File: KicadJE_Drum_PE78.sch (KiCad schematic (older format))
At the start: 112 parts, among them J101 Snare, J102 LCymbals, J103 SCymbals, J104 Maracas, J105 Bass, J106 LBongo, J107 HBongo, J108 Claves, P101 HEADER_2x8_Doepfer, Q101 2N3904, Q102 2N3904, Q103 2N3904, Q104 2N3904, U101 74HC04

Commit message: Faceplate etc
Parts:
- P101: footprint HEADER_2x8 -> Connector_IDC:IDC-Header_2x08_P2.54mm_Vertical
- U101: footprint AJ:AJ_SO-14_5.3x6.2mm_P1.27mm -> Package_SO:SO-14_5.3x10.2mm_P1.27mm
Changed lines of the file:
@@
 F 0 "U101" H 3875 1042 50  0000 C CNN
 F 1 "74HC04" H 3875 951 50  0000 C CNN
-F 2 "AJ:AJ_SO-14_5.3x6.2mm_P1.27mm" H 3875 725 50  0001 C CNN
+F 2 "Package_SO:SO-14_5.3x10.2mm_P1.27mm" H 3875 725 50  0001 C CNN
 F 3 "https://assets.nexperia.com/documents/data-sheet/74HC_HCT04.pdf" H 3875 725 50  0001 C CNN
 	1    3875 725
@@
 F 0 "U101" H 8500 1042 50  0000 C CNN
 F 1 "74HC04" H 8500 951 50  0000 C CNN
-F 2 "AJ:AJ_SO-14_5.3x6.2mm_P1.27mm" H 8500 725 50  0001 C CNN
+F 2 "Package_SO:SO-14_5.3x10.2mm_P1.27mm" H 8500 725 50  0001 C CNN
 F 3 "https://assets.nexperia.com/documents/data-sheet/74HC_HCT04.pdf" H 8500 725 50  0001 C CNN
 	2    8500 725
@@
 F 0 "U101" H 3875 2867 50  0000 C CNN
 F 1 "74HC04" H 3875 2776 50  0000 C CNN
-F 2 "AJ:AJ_SO-14_5.3x6.2mm_P1.27mm" H 3875 2550 50  0001 C CNN
+F 2 "Package_SO:SO-14_5.3x10.2mm_P1.27mm" H 3875 2550 50  0001 C CNN
 F 3 "https://assets.nexperia.com/documents/data-sheet/74HC_HCT04.pdf" H 3875 2550 50  0001 C CNN
 	3    3875 2550
@@
 F 0 "U101" H 8450 2842 50  0000 C CNN
 F 1 "74HC04" H 8450 2751 50  0000 C CNN
-F 2 "AJ:AJ_SO-14_5.3x6.2mm_P1.27mm" H 8450 2525 50  0001 C CNN
+F 2 "Package_SO:SO-14_5.3x10.2mm_P1.27mm" H 8450 2525 50  0001 C CNN
 F 3 "https://assets.nexperia.com/documents/data-sheet/74HC_HCT04.pdf" H 8450 2525 50  0001 C CNN
 	4    8450 2525
@@
 F 0 "U101" H 10905 5621 50  0000 L CNN
 F 1 "74HC04" H 10905 5530 50  0000 L CNN
-F 2 "AJ:AJ_SO-14_5.3x6.2mm_P1.27mm" H 10675 5575 50  0001 C CNN
+F 2 "Package_SO:SO-14_5.3x10.2mm_P1.27mm" H 10675 5575 50  0001 C CNN
 F 3 "https://assets.nexperia.com/documents/data-sheet/74HC_HCT04.pdf" H 10675 5575 50  0001 C CNN
 	7    10675 5575
@@
 F 0 "P101" H 8025 4977 40  0000 C CNN
 F 1 "HEADER_2x8_Doepfer" H 8025 5053 40  0000 C CNN
-F 2 "HEADER_2x8" H 8025 5144 60  0000 C CNN
+F 2 "Connector_IDC:IDC-Header_2x08_P2.54mm_Vertical" H 8025 5144 60  0000 C CNN
 F 3 "" H 8025 5675 60  0000 C CNN
 	1    8025 5675

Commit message: Powerfootprintupdated
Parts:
- C101, C102, C103, C104, C105, C106, C107, C108, C109, C110, C111, C112, C113, C114, C115, C116, C117, C118, C119, C120, C121, C122, C123, C124, C125, C126, C127, C128, C129, C130: footprint Capacitor_SMD:C_1206_3216Metric_Pad1.42x1.75mm_HandSolder -> AJ:C_0805_AJ
- RV102: value R_POT -> 220k
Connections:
- net -12: now reaches D109.1 (K), P101.1 (-12), P101.2 (-12), R145.2
- net +12: now reaches P101.10 (+12), P101.9 (+12), R151.2
- net +5: now reaches P101.11 (+5), P101.12 (+5), R146.2
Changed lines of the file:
@@
 F 0 "C128" H 8890 6021 50  0000 L CNN
 F 1 "1u" H 8890 5930 50  0000 L CNN
-F 2 "Capacitor_SMD:C_1206_3216Metric_Pad1.42x1.75mm_HandSolder" H 8813 5825 50  0001 C CNN
+F 2 "AJ:C_0805_AJ" H 8813 5825 50  0001 C CNN
 F 3 "~" H 8775 5975 50  0001 C CNN
 	1    8775 5975
@@
 F 0 "C127" H 8890 5621 50  0000 L CNN
 F 1 "1u" H 8890 5530 50  0000 L CNN
-F 2 "Capacitor_SMD:C_1206_3216Metric_Pad1.42x1.75mm_HandSolder" H 8813 5425 50  0001 C CNN
+F 2 "AJ:C_0805_AJ" H 8813 5425 50  0001 C CNN
 F 3 "~" H 8775 5575 50  0001 C CNN
 	1    8775 5575
@@
 F 0 "C113" H 3940 1546 50  0000 L CNN
 F 1 "150n" H 3940 1455 50  0000 L CNN
-F 2 "Capacitor_SMD:C_1206_3216Metric_Pad1.42x1.75mm_HandSolder" H 3863 1350 50  0001 C CNN
+F 2 "AJ:C_0805_AJ" H 3863 1350 50  0001 C CNN
 F 3 "~" H 3825 1500 50  0001 C CNN
 	1    3825 1500
@@
 F 0 "C109" H 3690 1871 50  0000 L CNN
 F 1 "47n" H 3690 1780 50  0000 L CNN
-F 2 "Capacitor_SMD:C_1206_3216Metric_Pad1.42x1.75mm_HandSolder" H 3613 1675 50  0001 C CNN
+F 2 "AJ:C_0805_AJ" H 3613 1675 50  0001 C CNN
 F 3 "~" H 3575 1825 50  0001 C CNN
 	1    3575 1825
@@
 F 0 "C115" H 4140 1871 50  0000 L CNN
 F 1 "47n" H 4140 1780 50  0000 L CNN
-F 2 "Capacitor_SMD:C_1206_3216Metric_Pad1.42x1.75mm_HandSolder" H 4063 1675 50  0001 C CNN
+F 2 "AJ:C_0805_AJ" H 4063 1675 50  0001 C CNN
 F 3 "~" H 4025 1825 50  0001 C CNN
 	1    4025 1825
@@
 F 0 "C123" H 8540 1546 50  0000 L CNN
 F 1 "33n" H 8540 1455 50  0000 L CNN
-F 2 "Capacitor_SMD:C_1206_3216Metric_Pad1.42x1.75mm_HandSolder" H 8463 1350 50  0001 C CNN
+F 2 "AJ:C_0805_AJ" H 8463 1350 50  0001 C CNN
 F 3 "~" H 8425 1500 50  0001 C CNN
 	1    8425 1500
@@
 F 0 "C121" H 8290 1871 50  0000 L CNN
 F 1 "10n" H 8290 1780 50  0000 L CNN
-F 2 "Capacitor_SMD:C_1206_3216Metric_Pad1.42x1.75mm_HandSolder" H 8213 1675 50  0001 C CNN
+F 2 "AJ:C_0805_AJ" H 8213 1675 50  0001 C CNN
 F 3 "~" H 8175 1825 50  0001 C CNN
 	1    8175 1825
@@
 F 0 "C125" H 8740 1871 50  0000 L CNN
 F 1 "10n" H 8740 1780 50  0000 L CNN
-F 2 "Capacitor_SMD:C_1206_3216Metric_Pad1.42x1.75mm_HandSolder" H 8663 1675 50  0001 C CNN
+F 2 "AJ:C_0805_AJ" H 8663 1675 50  0001 C CNN
 F 3 "~" H 8625 1825 50  0001 C CNN
 	1    8625 1825
@@
 F 0 "C124" H 8540 3346 50  0000 L CNN
 F 1 "4n7" H 8540 3255 50  0000 L CNN
-F 2 "Capacitor_SMD:C_1206_3216Metric_Pad1.42x1.75mm_HandSolder" H 8463 3150 50  0001 C CNN
+F 2 "AJ:C_0805_AJ" H 8463 3150 50  0001 C CNN
 F 3 "~" H 8425 3300 50  0001 C CNN
 	1    8425 3300
@@
 F 0 "C122" H 8290 3671 50  0000 L CNN
 F 1 "1n5" H 8290 3580 50  0000 L CNN
-F 2 "Capacitor_SMD:C_1206_3216Metric_Pad1.42x1.75mm_HandSolder" H 8213 3475 50  0001 C CNN
+F 2 "AJ:C_0805_AJ" H 8213 3475 50  0001 C CNN
 F 3 "~" H 8175 3625 50  0001 C CNN
 	1    8175 3625
@@
 F 0 "C126" H 8740 3671 50  0000 L CNN
 F 1 "1n5" H 8740 3580 50  0000 L CNN
-F 2 "Capacitor_SMD:C_1206_3216Metric_Pad1.42x1.75mm_HandSolder" H 8663 3475 50  0001 C CNN
+F 2 "AJ:C_0805_AJ" H 8663 3475 50  0001 C CNN
 F 3 "~" H 8625 3625 50  0001 C CNN
 	1    8625 3625
@@
 F 0 "C114" H 3940 3371 50  0000 L CNN
 F 1 "47n" H 3940 3280 50  0000 L CNN
-F 2 "Capacitor_SMD:C_1206_3216Metric_Pad1.42x1.75mm_HandSolder" H 3863 3175 50  0001 C CNN
+F 2 "AJ:C_0805_AJ" H 3863 3175 50  0001 C CNN
 F 3 "~" H 3825 3325 50  0001 C CNN
 	1    3825 3325
@@
 F 0 "C110" H 3690 3696 50  0000 L CNN
 F 1 "15n" H 3690 3605 50  0000 L CNN
-F 2 "Capacitor_SMD:C_1206_3216Metric_Pad1.42x1.75mm_HandSolder" H 3613 3500 50  0001 C CNN
+F 2 "AJ:C_0805_AJ" H 3613 3500 50  0001 C CNN
 F 3 "~" H 3575 3650 50  0001 C CNN
 	1    3575 3650
@@
 F 0 "C116" H 4140 3696 50  0000 L CNN
 F 1 "15n" H 4140 3605 50  0000 L CNN
-F 2 "Capacitor_SMD:C_1206_3216Metric_Pad1.42x1.75mm_HandSolder" H 4063 3500 50  0001 C CNN
+F 2 "AJ:C_0805_AJ" H 4063 3500 50  0001 C CNN
 F 3 "~" H 4025 3650 50  0001 C CNN
 	1    4025 3650
@@
 F 0 "C104" H 1890 946 50  0000 L CNN
 F 1 "150n" H 1890 855 50  0000 L CNN
-F 2 "Capacitor_SMD:C_1206_3216Metric_Pad1.42x1.75mm_HandSolder" H 1813 750 50  0001 C CNN
+F 2 "AJ:C_0805_AJ" H 1813 750 50  0001 C CNN
 F 3 "~" H 1775 900 50  0001 C CNN
 	1    1775 900
@@
 F 0 "C118" H 6340 921 50  0000 L CNN
 F 1 "33n" H 6340 830 50  0000 L CNN
-F 2 "Capacitor_SMD:C_1206_3216Metric_Pad1.42x1.75mm_HandSolder" H 6263 725 50  0001 C CNN
+F 2 "AJ:C_0805_AJ" H 6263 725 50  0001 C CNN
 F 3 "~" H 6225 875 50  0001 C CNN
 	1    6225 875
@@
 F 0 "C105" H 1890 2771 50  0000 L CNN
 F 1 "47n" H 1890 2680 50  0000 L CNN
-F 2 "Capacitor_SMD:C_1206_3216Metric_Pad1.42x1.75mm_HandSolder" H 1813 2575 50  0001 C CNN
+F 2 "AJ:C_0805_AJ" H 1813 2575 50  0001 C CNN
 F 3 "~" H 1775 2725 50  0001 C CNN
 	1    1775 2725
@@
 F 0 "C119" H 6340 2746 50  0000 L CNN
 F 1 "4n7" H 6340 2655 50  0000 L CNN
-F 2 "Capacitor_SMD:C_1206_3216Metric_Pad1.42x1.75mm_HandSolder" H 6263 2550 50  0001 C CNN
+F 2 "AJ:C_0805_AJ" H 6263 2550 50  0001 C CNN
 F 3 "~" H 6225 2700 50  0001 C CNN
 	1    6225 2700
@@
 F 0 "C102" H 1715 4971 50  0000 L CNN
 F 1 "100n" H 1715 4880 50  0000 L CNN
-F 2 "Capacitor_SMD:C_1206_3216Metric_Pad1.42x1.75mm_HandSolder" H 1638 4775 50  0001 C CNN
+F 2 "AJ:C_0805_AJ" H 1638 4775 50  0001 C CNN
 F 3 "~" H 1600 4925 50  0001 C CNN
 	1    1600 4925
@@
 F 0 "C101" H 1565 5946 50  0000 L CNN
 F 1 "330n" H 1565 5855 50  0000 L CNN
-F 2 "Capacitor_SMD:C_1206_3216Metric_Pad1.42x1.75mm_HandSolder" H 1488 5750 50  0001 C CNN
+F 2 "AJ:C_0805_AJ" H 1488 5750 50  0001 C CNN
 F 3 "~" H 1450 5900 50  0001 C CNN
 	1    1450 5900
@@
 F 0 "C106" H 1965 6646 50  0000 L CNN
 F 1 "68n" H 1965 6555 50  0000 L CNN
-F 2 "Capacitor_SMD:C_1206_3216Metric_Pad1.42x1.75mm_HandSolder" H 1888 6450 50  0001 C CNN
+F 2 "AJ:C_0805_AJ" H 1888 6450 50  0001 C CNN
 F 3 "~" H 1850 6600 50  0001 C CNN
 	1    1850 6600
@@
 F 0 "C103" H 1715 7171 50  0000 L CNN
 F 1 "220n" H 1715 7080 50  0000 L CNN
-F 2 "Capacitor_SMD:C_1206_3216Metric_Pad1.42x1.75mm_HandSolder" H 1638 6975 50  0001 C CNN
+F 2 "AJ:C_0805_AJ" H 1638 6975 50  0001 C CNN
 F 3 "~" H 1600 7125 50  0001 C CNN
 	1    1600 7125
@@
 F 0 "C107" H 2740 7346 50  0000 L CNN
 F 1 "100n" H 2740 7255 50  0000 L CNN
-F 2 "Capacitor_SMD:C_1206_3216Metric_Pad1.42x1.75mm_HandSolder" H 2663 7150 50  0001 C CNN
+F 2 "AJ:C_0805_AJ" H 2663 7150 50  0001 C CNN
 F 3 "~" H 2625 7300 50  0001 C CNN
 	1    2625 7300
@@
 F 0 "C108" H 3165 5621 50  0000 L CNN
 F 1 "68n" H 3165 5530 50  0000 L CNN
-F 2 "Capacitor_SMD:C_1206_3216Metric_Pad1.42x1.75mm_HandSolder" H 3088 5425 50  0001 C CNN
+F 2 "AJ:C_0805_AJ" H 3088 5425 50  0001 C CNN
 F 3 "~" H 3050 5575 50  0001 C CNN
 	1    3050 5575
@@
 F 0 "C111" H 3765 5346 50  0000 L CNN
 F 1 "4n7" H 3765 5255 50  0000 L CNN
-F 2 "Capacitor_SMD:C_1206_3216Metric_Pad1.42x1.75mm_HandSolder" H 3688 5150 50  0001 C CNN
+F 2 "AJ:C_0805_AJ" H 3688 5150 50  0001 C CNN
 F 3 "~" H 3650 5300 50  0001 C CNN
 	1    3650 5300
@@
 F 0 "C112" H 3915 5996 50  0000 L CNN
 F 1 "4n7" H 3915 5905 50  0000 L CNN
-F 2 "Capacitor_SMD:C_1206_3216Metric_Pad1.42x1.75mm_HandSolder" H 3838 5800 50  0001 C CNN
+F 2 "AJ:C_0805_AJ" H 3838 5800 50  0001 C CNN
 F 3 "~" H 3800 5950 50  0001 C CNN
 	1    3800 5950
@@
 F 0 "C117" H 4940 5871 50  0000 L CNN
 F 1 "22n" H 4940 5780 50  0000 L CNN
-F 2 "Capacitor_SMD:C_1206_3216Metric_Pad1.42x1.75mm_HandSolder" H 4863 5675 50  0001 C CNN
+F 2 "AJ:C_0805_AJ" H 4863 5675 50  0001 C CNN
 F 3 "~" H 4825 5825 50  0001 C CNN
 	1    4825 5825
@@
 F 0 "C120" H 6415 6421 50  0000 L CNN
 F 1 "100n" H 6415 6330 50  0000 L CNN
-F 2 "Capacitor_SMD:C_1206_3216Metric_Pad1.42x1.75mm_HandSolder" H 6338 6225 50  0001 C CNN
+F 2 "AJ:C_0805_AJ" H 6338 6225 50  0001 C CNN
 F 3 "~" H 6300 6375 50  0001 C CNN
 	1    6300 6375
@@
 P 5475 6375
 F 0 "RV102" H 5406 6421 50  0000 R CNN
-F 1 "R_POT" H 5406 6330 50  0000 R CNN
+F 1 "220k" H 5406 6330 50  0000 R CNN
 F 2 "AJ:Potentiometer_China_RK09_Single_Vertical_AJ" H 5475 6375 50  0001 C CNN
 F 3 "~" H 5475 6375 50  0001 C CNN
@@
 F 0 "C129" H 8965 4996 50  0000 L CNN
 F 1 "1u" H 8965 4905 50  0000 L CNN
-F 2 "Capacitor_SMD:C_1206_3216Metric_Pad1.42x1.75mm_HandSolder" H 8888 4800 50  0001 C CNN
+F 2 "AJ:C_0805_AJ" H 8888 4800 50  0001 C CNN
 F 3 "~" H 8850 4950 50  0001 C CNN
 	1    8850 4950
@@
 F 0 "C130" H 9315 4996 50  0000 L CNN
 F 1 "100n" H 9315 4905 50  0000 L CNN
-F 2 "Capacitor_SMD:C_1206_3216Metric_Pad1.42x1.75mm_HandSolder" H 9238 4800 50  0001 C CNN
+F 2 "AJ:C_0805_AJ" H 9238 4800 50  0001 C CNN
 F 3 "~" H 9200 4950 50  0001 C CNN
 	1    9200 4950
@@
 Wire Wire Line
 	9000 4800 9200 4800
+Text Label 7675 5575 0    50   ~ 0
++12
+Text Label 7675 5975 0    50   ~ 0
+-12
+Text Label 7675 5475 0    50   ~ 0
++5
 $EndSCHEMATC

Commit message: AC coupled noise
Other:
- note removed: "HUSK NU AT LAVE +5V !!!!!!!!!!"
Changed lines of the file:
@@
 Wire Wire Line
 	10675 6150 10675 6075
-Text Notes 5000 8950 0    157  ~ 0
-HUSK NU AT LAVE +5V !!!!!!!!!!
 $Comp
 L Device:C C101

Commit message: Power to TL072
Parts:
- added U302: TL072, AJ:AJ_SO-8_5.3x6.2mm_P1.27mm, symbol Amplifier_Operational:TL072
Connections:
- net +12Vc: now also U302.8 (V+)
- net -12Vc: now also U302.4 (V-)
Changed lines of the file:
@@
 Text Label 7675 5475 0    50   ~ 0
 +5
+$Comp
+L Amplifier_Operational:TL072 U?
+U 3 1 608BB6D8
+P 9725 5750
+AR Path="/6165D4D0/608BB6D8" Ref="U?"  Part="2"
+AR Path="/608BB6D8" Ref="U302"  Part="3"
+F 0 "U302" H 9500 5600 50  0000 C CNN
+F 1 "TL072" H 9500 5750 50  0000 C CNN
+F 2 "AJ:AJ_SO-8_5.3x6.2mm_P1.27mm" H 9725 5750 50  0001 C CNN
+F 3 "http://www.ti.com/lit/ds/symlink/tl071.pdf" H 9725 5750 50  0001 C CNN
+	3    9725 5750
+	-1   0    0    -1
+$EndComp
+Wire Wire Line
+	9825 6175 9825 6050
+Wire Wire Line
+	9825 5450 9825 5375
 $EndSCHEMATC

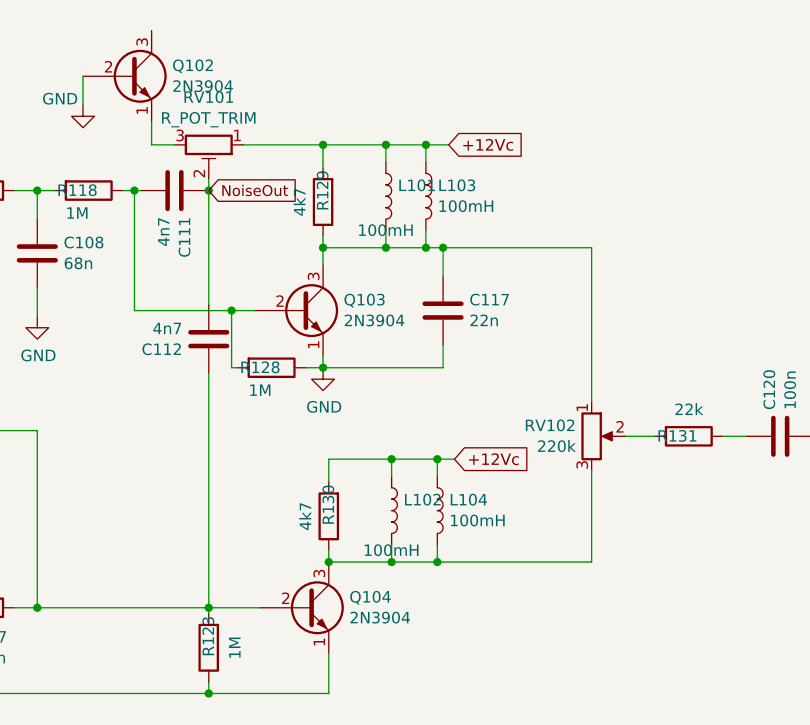
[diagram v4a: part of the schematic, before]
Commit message: THT Coils removed
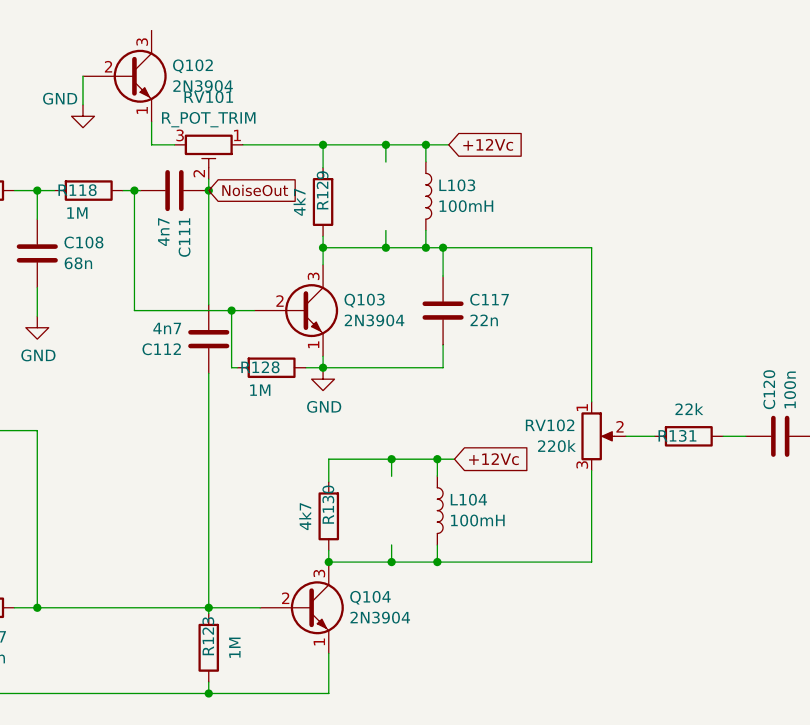
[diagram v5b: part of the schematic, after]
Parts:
- removed L101, L102: 100mH, Inductor_THT:L_Radial_D7.5mm_P3.50mm_Fastron_07P, symbol Device:L
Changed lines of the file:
@@
 	0    -1   -1   0
-$EndComp
-$Comp
-L Device:L L101
-U 1 1 6121074D
-P 4575 5325
-F 0 "L101" H 4627 5371 50  0000 L CNN
-F 1 "100mH" H 4450 5175 50  0000 L CNN
-F 2 "Inductor_THT:L_Radial_D7.5mm_P3.50mm_Fastron_07P" H 4575 5325 50  0001 C CNN
-F 3 "~" H 4575 5325 50  0001 C CNN
-	1    4575 5325
-	1    0    0    -1
 $EndComp
 Wire Wire Line
@@
 Wire Wire Line
 	4325 6475 4600 6475
-$Comp
-L Device:L L102
-U 1 1 6122F538
-P 4600 6700
-F 0 "L102" H 4652 6746 50  0000 L CNN
-F 1 "100mH" H 4475 6525 50  0000 L CNN
-F 2 "Inductor_THT:L_Radial_D7.5mm_P3.50mm_Fastron_07P" H 4600 6700 50  0001 C CNN
-F 3 "~" H 4600 6700 50  0001 C CNN
-	1    4600 6700
-	1    0    0    -1
-$EndComp
 Wire Wire Line
 	4600 6925 4600 6850

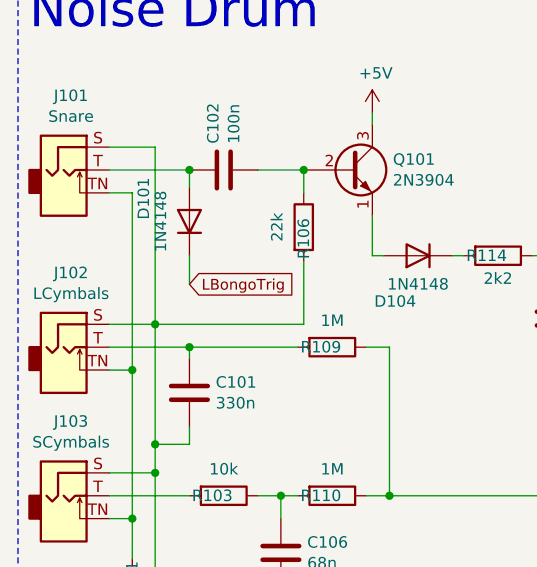
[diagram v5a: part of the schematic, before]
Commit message: BB Logo - GND planes
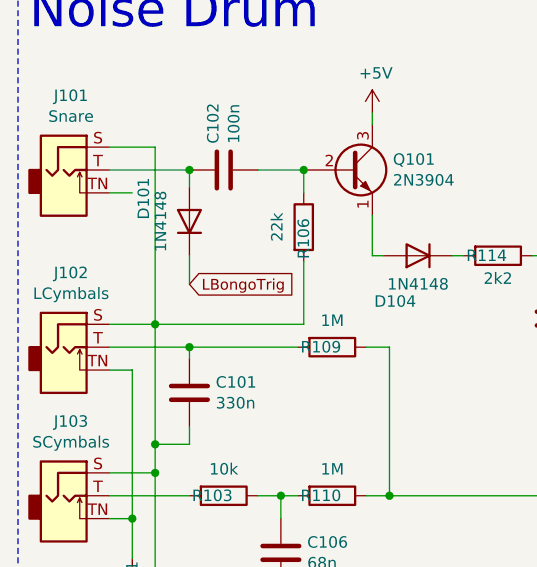
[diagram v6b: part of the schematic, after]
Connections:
- net at J102.TN, J103.TN, R101.2: no longer J101.TN
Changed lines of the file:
@@
 Wire Wire Line
 	1100 5800 1200 5800
-Connection ~ 1200 5800
-Wire Wire Line
-	1200 5800 1200 5025
 Wire Wire Line
 	1200 6450 1200 6625
